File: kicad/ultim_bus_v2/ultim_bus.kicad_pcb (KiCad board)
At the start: 2 copper layers, 198.1 x 55.9 mm, 90 parts, among them M1 MouseBite, M10 MouseBite, M11 MouseBite, M12 MouseBite, M13 MouseBite, M15 MouseBite, M16 MouseBite, M17 MouseBite, M18 MouseBite, M2 MouseBite, M3 MouseBite, M4 MouseBite, M5 MouseBite, M6 MouseBite, M8 MouseBite, M9 MouseBite, P1 CONN_1, P10 CONN_1, P11 CONN_1, P12 CONN_1, P13 CONN_1, P14 CONN_1, P15 CONN_1, P16 CONN_1, P17 CONN_1, P18 CONN_1, P19 CONN_1, P2 CONN_1, P20 CONN_1, P21 CONN_1, P22 CONN_1, P23 CONN_1, P24 CONN_1, P25 CONN_1, P26 CONN_1, P27 CONN_1, P28 CONN_1, P29 CONN_1, P3 CONN_1, P30 CONN_1, P31 CONN_1, P32 CONN_1, P33 CONN_1, P34 CONN_1, P35 CONN_1, P36 CONN_1, P37 CONN_1, P38 CONN_1, P39 CONN_1, P4 CONN_1, P40 CONN_1, P41 CONN_1, P42 CONN_1, P43 CONN_1, P44 CONN_1, P45 CONN_1, P46 CONN_1, P47 CONN_1, P48 CONN_1, P49 CONN_1, P5 CONN_1, P50 CONN_1, P51 CONN_1, P52 CONN_1, P6 CONN_1, P7 CONN_1, P8 CONN_1, P9 CONN_1

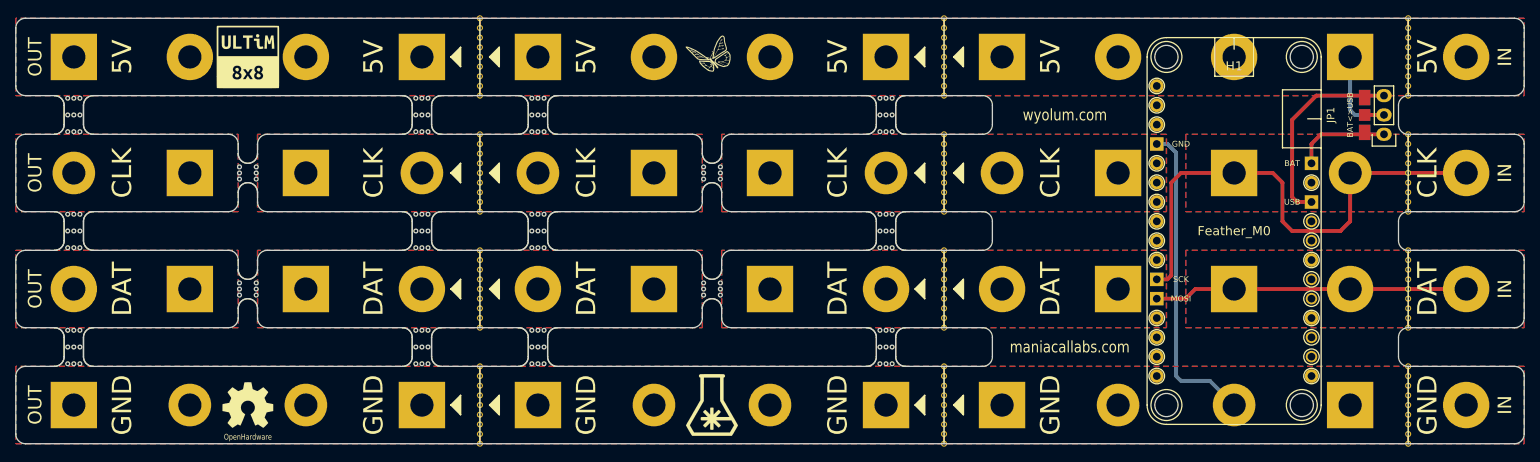
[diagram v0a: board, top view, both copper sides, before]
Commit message: added 6 SMD switches to ultim_bus_v2 with pullup resistors
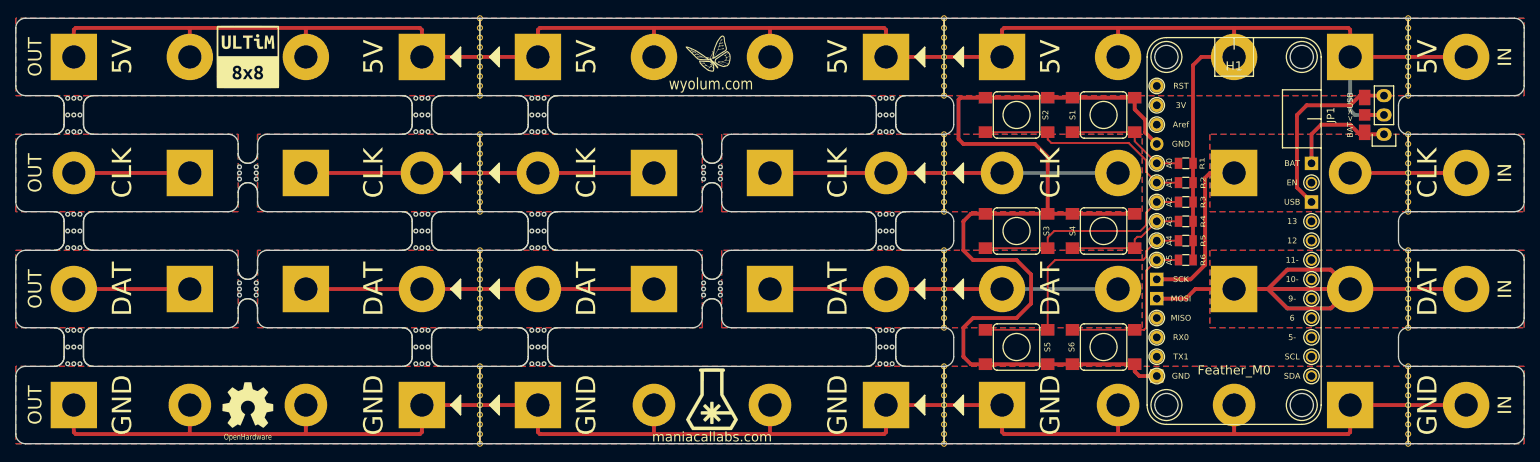
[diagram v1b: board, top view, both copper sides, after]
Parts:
- added R1: 10k, ultim_bus:r_0805, F.Cu at (181.6, 44.5)
- added R2: 10k, ultim_bus:r_0805, F.Cu at (181.6, 47.0)
- added R3: 10k, ultim_bus:r_0805, F.Cu at (181.6, 49.5)
- added R4: 10k, ultim_bus:r_0805, F.Cu at (181.6, 52.1)
- added R5: 10k, ultim_bus:r_0805, F.Cu at (181.6, 54.6)
- added R6: 10k, ultim_bus:r_0805, F.Cu at (181.6, 57.1)
- added S1: SPST-M-2, ultim_bus:SW_SMD, F.Cu at (170.8, 38.1)
- added S2: SPST-M-2, ultim_bus:SW_SMD, F.Cu at (159.4, 38.1)
- added S3: SPST-M-2, ultim_bus:SW_SMD, F.Cu at (159.4, 53.3)
- added S4: SPST-M-2, ultim_bus:SW_SMD, F.Cu at (170.8, 53.3)
- added S5: SPST-M-2, ultim_bus:SW_SMD, F.Cu at (159.4, 68.6)
- added S6: SPST-M-2, ultim_bus:SW_SMD, F.Cu at (170.8, 68.6)
- moved L7 0.76 mm to (119.4, 75.4)
- moved L8 0.76 mm to (119.4, 75.4)
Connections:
- H1 pad 10: (no net) -> /VUSB
- H1 pad 11: /CLK -> (no net)
- H1 pad 12: /DAT -> /VBAT
- H1 pad 16: (no net) -> /GND
- H1 pad 17: (no net) -> /A0
- H1 pad 18: (no net) -> /A1
- H1 pad 19: (no net) -> /A2
- H1 pad 20: (no net) -> /A3
- H1 pad 21: (no net) -> /A4
- H1 pad 22: (no net) -> /A5
- H1 pad 23: (no net) -> /CLK
- H1 pad 24: (no net) -> /DAT
- H1 pad 26: /VUSB -> (no net)
- H1 pad 28: /VBAT -> /GND
- H1 pad 4: /GND -> (no net)
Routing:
- net /GND: track 49.2 -> 375.0 mm
- net /5V: track 21.9 -> 281.0 mm
- net /DAT: track 43.7 -> 128.3 mm
- net /DAT2: track 2.54 -> 48.3 mm
- net /DAT1: track 2.54 -> 48.3 mm
- net /CLK2: track 2.54 -> 48.3 mm
- net /CLK1: track 2.54 -> 48.3 mm
- net /A4: track 0.00 -> 35.5 mm
- net /A2: track 0.00 -> 29.7 mm
- net /A1: track 0.00 -> 29.6 mm
- net /CLK: track 69.1 -> 40.4 mm
- net /A5: track 0.00 -> 22.7 mm
- net /A0: track 0.00 -> 16.4 mm
- net /A3: track 0.00 -> 16.1 mm
- net /DAT3: track 0.00 -> 15.2 mm
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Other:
- outline, holes or cut-outs redrawn
